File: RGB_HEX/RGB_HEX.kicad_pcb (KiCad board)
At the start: 2 copper layers, 47.8 x 41.3 mm, 46 parts, among them IC1 ATMEGA328P-M, P1 I2C, P2 FTDI, P3 ISP, Q1 NPN, Q2 NPN, Q3 NPN, Q4 NPN, Q5 NPN, Q6 NPN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

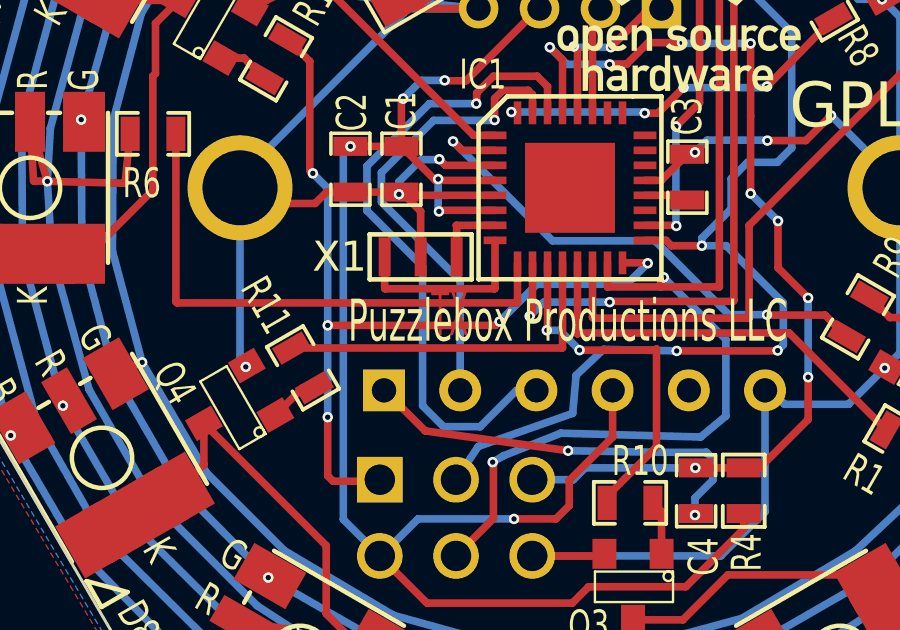
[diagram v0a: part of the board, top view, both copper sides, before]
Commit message: fixed bugs on NPN and PNP library, IR module and Pyramid Shield
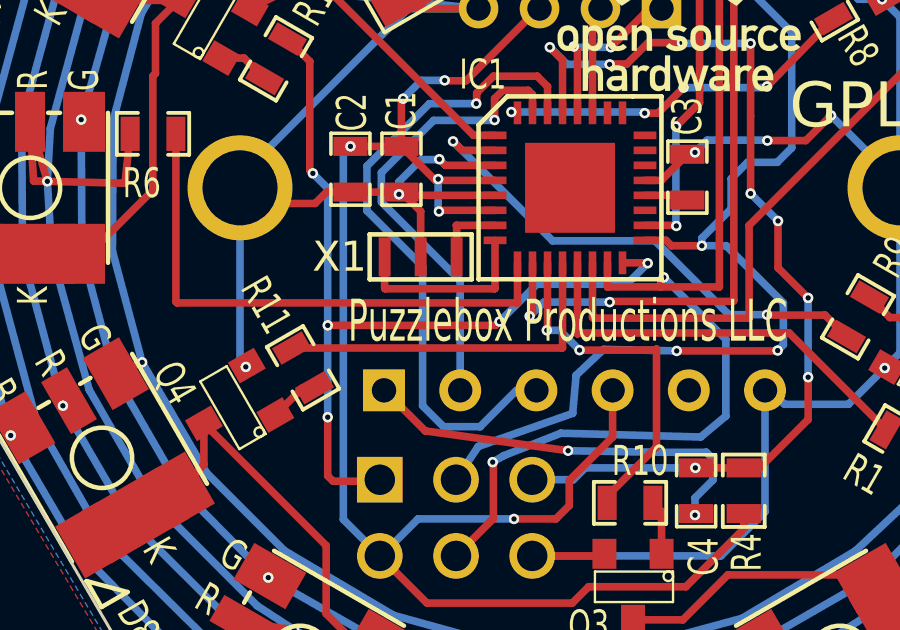
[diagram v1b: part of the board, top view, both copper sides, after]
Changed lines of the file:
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@@
     (area -24.4983 -22.2072 24.752301 22.2072)
     (thickness 1.6)
-    (drawings 30)
+    (drawings 29)
     (tracks 692)
     (zones 0)
@@
   )
   (layers
-    (15 F.Cu signal hide)
+    (15 F.Cu signal)
     (0 B.Cu signal hide)
-    (16 B.Adhes user)
-    (17 F.Adhes user)
+    (16 B.Adhes user hide)
+    (17 F.Adhes user hide)
     (18 B.Paste user)
-    (19 F.Paste user)
-    (20 B.SilkS user)
+    (19 F.Paste user hide)
+    (20 B.SilkS user hide)
     (21 F.SilkS user hide)
     (22 B.Mask user hide)
@@
     (visible_elements 7FFFFFBF)
     (pcbplotparams
-      (layerselection 272400385)
+      (layerselection 284983297)
       (usegerberextensions true)
       (excludeedgelayer true)
@@
     (effects (font (size 1.5 0.7) (thickness 0.15)) (justify mirror))
   )
-  (gr_text TX (at -4.0005 4.2164) (layer F.Cu)
-    (effects (font (size 1.5 0.7) (thickness 0.175)))
-  )
   (gr_circle (center 0 0) (end 0 -19.4) (layer Cmts.User) (width 0.2))

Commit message: New Product Importing
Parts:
- C2, C3, C4: value 0.1uF -> 100nF
- R1, R5: value 13k -> 1.0k 1%
- R2, R6: value 15k -> 1.2k 1%
- R3, R7: value 27k -> 2.1k 1%
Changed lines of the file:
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@@
   (layers
     (15 F.Cu signal)
-    (0 B.Cu signal hide)
-    (16 B.Adhes user hide)
-    (17 F.Adhes user hide)
+    (0 B.Cu signal)
+    (16 B.Adhes user)
+    (17 F.Adhes user)
     (18 B.Paste user)
-    (19 F.Paste user hide)
-    (20 B.SilkS user hide)
-    (21 F.SilkS user hide)
-    (22 B.Mask user hide)
+    (19 F.Paste user)
+    (20 B.SilkS user)
+    (21 F.SilkS user)
+    (22 B.Mask user)
     (23 F.Mask user)
     (24 Dwgs.User user)
@@
       (effects (font (size 1 0.7) (thickness 0.15)))
     )
-    (fp_text value 27k (at 0.0254 0.1016 60) (layer F.SilkS) hide
+    (fp_text value "2.1k 1%" (at 0.0254 0.1016 60) (layer F.SilkS) hide
       (effects (font (size 1 0.7) (thickness 0.15)))
     )
@@
     (tags "CMS Plcc")
     (attr smd)
-    (fp_text reference IC1 (at -2.9083 -3.7719) (layer F.SilkS)
+    (fp_text reference IC1 (at -2.159 -4.064) (layer F.SilkS)
       (effects (font (size 1 0.7) (thickness 0.15)))
     )
@@
       (effects (font (size 1 0.7) (thickness 0.15)))
     )
-    (fp_text value 15k (at 0.0254 0.1016 180) (layer F.SilkS) hide
+    (fp_text value "1.2k 1%" (at 0.0254 0.1016 180) (layer F.SilkS) hide
       (effects (font (size 1 0.7) (thickness 0.15)))
     )
@@
       (effects (font (size 1 0.7) (thickness 0.15)))
     )
-    (fp_text value 13k (at 0.0254 0.1016 120) (layer F.SilkS) hide
+    (fp_text value "1.0k 1%" (at 0.0254 0.1016 120) (layer F.SilkS) hide
       (effects (font (size 1 0.7) (thickness 0.15)))
     )
@@
       (effects (font (size 1 0.7) (thickness 0.15)))
     )
-    (fp_text value 15k (at 0.0254 0.1016 30) (layer F.SilkS) hide
+    (fp_text value "1.2k 1%" (at 0.0254 0.1016 30) (layer F.SilkS) hide
       (effects (font (size 1 0.7) (thickness 0.15)))
     )
@@
       (effects (font (size 1 0.7) (thickness 0.15)))
     )
-    (fp_text value 13k (at 0.0254 0.1016 330) (layer F.SilkS) hide
+    (fp_text value "1.0k 1%" (at 0.0254 0.1016 330) (layer F.SilkS) hide
       (effects (font (size 1 0.7) (thickness 0.15)))
     )
@@
       (effects (font (size 1 0.7) (thickness 0.15)))
     )
-    (fp_text value 27k (at 0.0254 0.1016 90) (layer F.SilkS) hide
+    (fp_text value "2.1k 1%" (at 0.0254 0.1016 90) (layer F.SilkS) hide
       (effects (font (size 1 0.7) (thickness 0.15)))
     )
@@
       (effects (font (size 1 0.7) (thickness 0.15)))
     )
-    (fp_text value 0.1uF (at 0.0508 0.0762 90) (layer F.SilkS) hide
+    (fp_text value 100nF (at 0.0254 1.7399 90) (layer F.SilkS) hide
       (effects (font (size 1 0.7) (thickness 0.15)))
     )
@@
       (effects (font (size 1 0.7) (thickness 0.15)))
     )
-    (fp_text value 0.1uF (at 0.0508 0.0762 270) (layer F.SilkS) hide
+    (fp_text value 100nF (at -0.3954 1.3805 270) (layer F.SilkS)
       (effects (font (size 1 0.7) (thickness 0.15)))
     )
@@
       (effects (font (size 1 0.7) (thickness 0.15)))
     )
-    (fp_text value 10uF (at 0.0508 0.0762 270) (layer F.SilkS) hide
+    (fp_text value 10uF (at -2.5544 -1.3645 270) (layer F.SilkS)
       (effects (font (size 1 0.7) (thickness 0.15)))
     )
@@
       (effects (font (size 1 0.7) (thickness 0.15)))
     )
-    (fp_text value 0.1uF (at 0.0508 0.0762 270) (layer F.SilkS) hide
+    (fp_text value 100nF (at 4.5085 -0.0508 270) (layer F.SilkS)
       (effects (font (size 1 0.7) (thickness 0.15)))
     )
@@
       (xy 3.15722 -1.10998) (xy 3.15722 -1.016) (xy 3.15722 -1.016)) (layer F.SilkS) (width 0.00254))
   )
-  (gr_text Puzzlebox.info (at 10.2743 -12.3698) (layer B.SilkS)
+  (gr_text Puzzlebox.info (at 14.224 -4.826) (layer B.SilkS)
     (effects (font (size 1.3 1) (thickness 0.25)) (justify mirror))
   )
